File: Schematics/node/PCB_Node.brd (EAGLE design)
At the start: 35.9 x 41.3 mm, 30 parts, among them U1 ATMEGA328P, U2 MAX485CSA+, U3 MCP1824ST-3302E/DB, Y2 16MHz

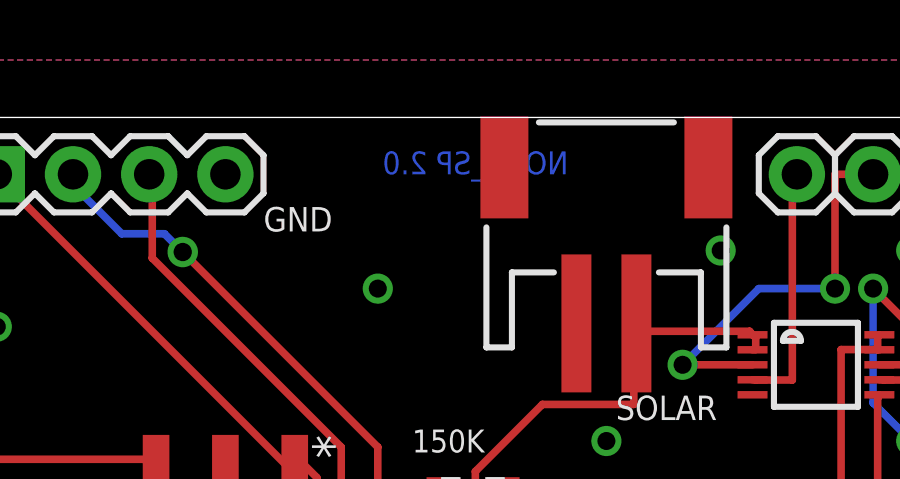
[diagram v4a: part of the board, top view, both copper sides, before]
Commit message: PCB improvements
Node_SP 2.0: moved some text to the back layer

Sen_SP 4.0: improved the board for programming and changed the
resonator from through hole to surface mount - then rearranged the
items on the board to make it smaller
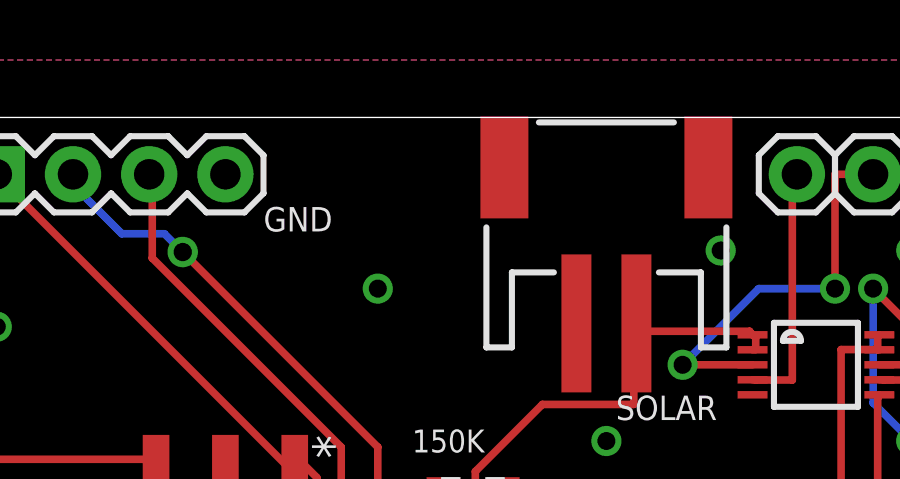
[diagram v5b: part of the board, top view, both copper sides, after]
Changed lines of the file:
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@@
 <text x="19.685" y="18.415" size="0.8128" layer="25">10k</text>
 <text x="16.51" y="12.7" size="1.778" layer="25">*</text>
-<text x="21.59" y="39.37" size="0.762" layer="16" ratio="18" rot="MR0">NODE_SP 2.0</text>
+<text x="21.59" y="39.37" size="0.762" layer="26" ratio="18" rot="MR0">NODE_SP 2.0</text>
 <text x="35.56" y="36.83" size="0.8128" layer="26" rot="MR0">PWR</text>
 <text x="32.385" y="36.83" size="0.8128" layer="26" rot="MR0">St2</text>
